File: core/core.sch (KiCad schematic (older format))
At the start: 9 parts, among them U1 BNO055

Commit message: Updated core with IMU and altimiter as specified on pinout
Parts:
- added C15, C16: 100nF, symbol Device:C
- added NT1: Net-Tie_2, symbol Device:Net-Tie_2
- added R6, R7: 4.7k, symbol Device:R
- added U3: BMP388, calstar:BMP388, symbol calstar:BMP388
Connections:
- net labels added: +3.3V, CSB, INT_ALT, INT_IMU
- net labels removed: INT, VDD, VDDIO
- wire segments 51 -> 89
- no-connect marks 52 -> 47
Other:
- moved on the sheet: C3, R2

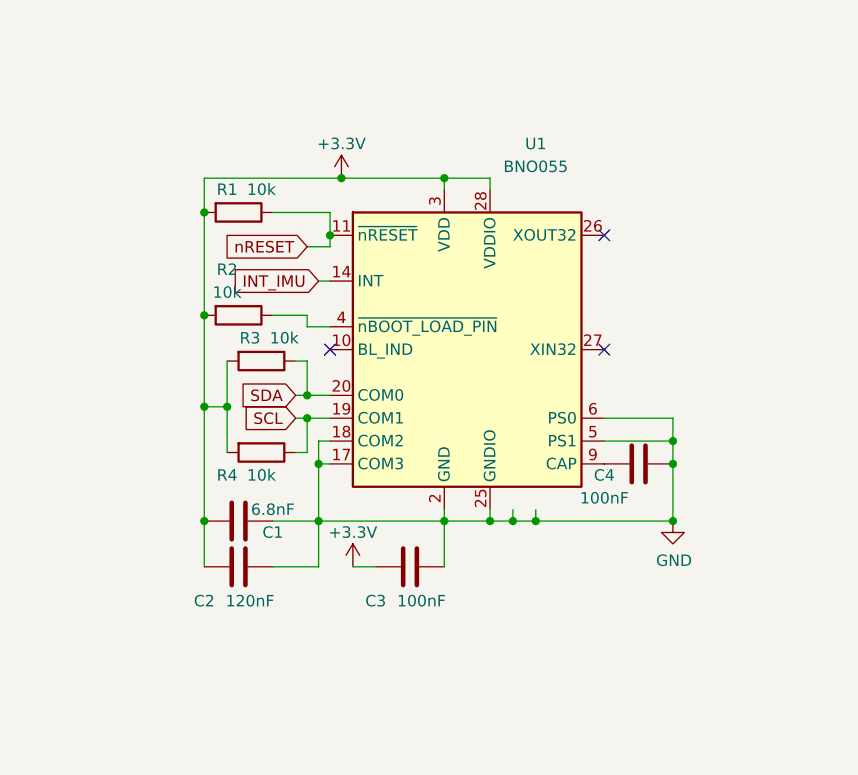
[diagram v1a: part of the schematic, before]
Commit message: Updated core with IMU hierarchical block
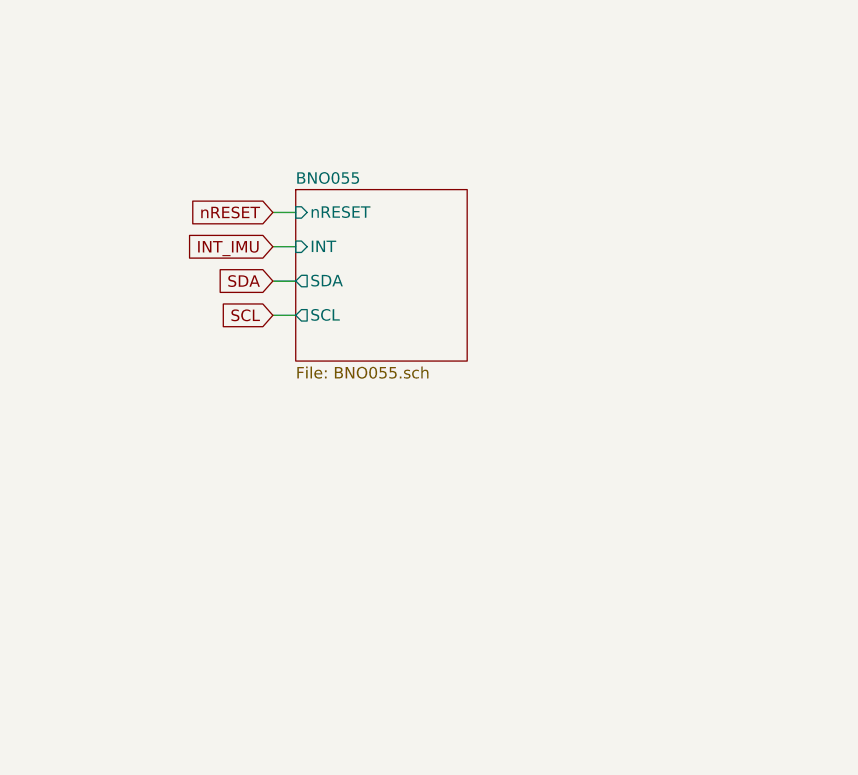
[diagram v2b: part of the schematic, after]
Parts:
- removed C1: 6.8nF, Capacitor_SMD:C_0603_1608Metric, symbol Device:C
- removed C2: 120nF, Capacitor_SMD:C_0603_1608Metric, symbol Device:C
- removed C3, C4: 100nF, Capacitor_SMD:C_0603_1608Metric, symbol Device:C
- removed R1, R2, R3, R4: 10k, Resistor_SMD:R_0603_1608Metric, symbol Device:R
- removed U1: BNO055, Package_LGA:LGA-28_5.2x3.8mm_P0.5mm, symbol Sensor_Motion:BNO055
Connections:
- wire segments 89 -> 41
- no-connect marks 47 -> 44

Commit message: Updated core with altimeter hierarchical block
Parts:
- removed C15, C16: 100nF, symbol Device:C
- removed NT1: Net-Tie_2, symbol Device:Net-Tie_2
- removed R6, R7: 4.7k, symbol Device:R
- removed U3: BMP388, calstar:BMP388, symbol calstar:BMP388
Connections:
- net labels removed: +3.3V, GND
- wire segments 41 -> 14
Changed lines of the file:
@@
 $Descr A4 11693 8268
 encoding utf-8
-Sheet 1 3
+Sheet 1 4
 Title ""
 Date ""
@@
 NoConn ~ 7500 4900
 NoConn ~ 7500 5050
-$Comp
-L calstar:BMP388 U3
-U 1 1 5E642E69
-P 3000 5750
-F 0 "U3" H 3000 6225 50  0000 C CNN
-F 1 "BMP388" H 3000 6134 50  0000 C CNN
-F 2 "calstar:BMP388" H 3000 6300 50  0001 C CNN
-F 3 "" H 3000 6150 50  0001 C CNN
-	1    3000 5750
-	1    0    0    -1
-$EndComp
-$Comp
-L Device:Net-Tie_2 NT1
-U 1 1 5E6430B0
-P 3450 5700
-F 0 "NT1" H 3600 5850 50  0000 C CNN
-F 1 "Net-Tie_2" H 3550 5750 50  0000 C CNN
-F 2 "" H 3450 5700 50  0001 C CNN
-F 3 "~" H 3450 5700 50  0001 C CNN
-	1    3450 5700
-	1    0    0    -1
-$EndComp
-$Comp
-L Device:R R6
-U 1 1 5E64313E
-P 3400 6100
-F 0 "R6" H 3470 6146 50  0000 L CNN
-F 1 "4.7k" H 3470 6055 50  0000 L CNN
-F 2 "" V 3330 6100 50  0001 C CNN
-F 3 "~" H 3400 6100 50  0001 C CNN
-	1    3400 6100
-	1    0    0    -1
-$EndComp
-$Comp
-L power:GND #PWR0114
-U 1 1 5E6431CF
-P 3550 5700
-F 0 "#PWR0114" H 3550 5450 50  0001 C CNN
-F 1 "GND" H 3400 5650 50  0000 C CNN
-F 2 "" H 3550 5700 50  0001 C CNN
-F 3 "" H 3550 5700 50  0001 C CNN
-	1    3550 5700
-	1    0    0    -1
-$EndComp
-Wire Wire Line
-	3350 5800 3450 5800
-Wire Wire Line
-	3450 5800 3450 5850
-Wire Wire Line
-	3800 5850 3800 5800
-Wire Wire Line
-	3450 5850 3800 5850
-$Comp
-L Device:R R7
-U 1 1 5E644FB0
-P 3800 5650
-F 0 "R7" H 3870 5696 50  0000 L CNN
-F 1 "4.7k" H 3870 5605 50  0000 L CNN
-F 2 "" V 3730 5650 50  0001 C CNN
-F 3 "~" H 3800 5650 50  0001 C CNN
-	1    3800 5650
-	1    0    0    -1
-$EndComp
-Wire Wire Line
-	3350 5900 3400 5900
-Wire Wire Line
-	3400 5900 3400 5950
-Text GLabel 3500 5450 2    50   Output ~ 0
+Text GLabel 2900 5400 0    50   Input ~ 0
 CSB
-Wire Wire Line
-	3450 5600 3450 5450
-Wire Wire Line
-	3450 5450 3500 5450
-Text GLabel 3500 5200 2    50   Input ~ 0
+Text GLabel 2900 5250 0    50   Input ~ 0
 INT_ALT
-Wire Wire Line
-	3500 5200 3400 5200
-Wire Wire Line
-	3400 5500 3350 5500
-Text GLabel 3850 5850 2    50   Input ~ 0
+Text GLabel 2900 5550 0    50   Input ~ 0
 SDA
-Wire Wire Line
-	3850 5850 3800 5850
-Connection ~ 3800 5850
-Text GLabel 3550 5950 2    50   Input ~ 0
+Text GLabel 3700 5550 2    50   Input ~ 0
 SCL
-Wire Wire Line
-	3550 5950 3400 5950
-Connection ~ 3400 5950
-Wire Wire Line
-	3800 5500 3800 5450
-$Comp
-L Device:C C16
-U 1 1 5E66780A
-P 2400 5550
-F 0 "C16" H 2650 5500 50  0000 R CNN
-F 1 "100nF" H 2650 5650 50  0000 R CNN
-F 2 "" H 2438 5400 50  0001 C CNN
-F 3 "~" H 2400 5550 50  0001 C CNN
-	1    2400 5550
-	-1   0    0    1
-$EndComp
-Wire Wire Line
-	2650 5600 2550 5600
-Wire Wire Line
-	2550 5600 2550 5500
-Wire Wire Line
-	2400 5700 2450 5700
-$Comp
-L power:GND #PWR0117
-U 1 1 5E66C6EE
-P 2450 5700
-F 0 "#PWR0117" H 2450 5450 50  0001 C CNN
-F 1 "GND" H 2300 5650 50  0000 C CNN
-F 2 "" H 2450 5700 50  0001 C CNN
-F 3 "" H 2450 5700 50  0001 C CNN
-	1    2450 5700
-	1    0    0    -1
-$EndComp
-Connection ~ 2450 5700
-Wire Wire Line
-	2450 5700 2650 5700
-Wire Wire Line
-	2650 5800 2550 5800
-Wire Wire Line
-	2550 5800 2550 5900
-Wire Wire Line
-	2550 5900 2650 5900
-Wire Wire Line
-	2550 5900 2250 5900
-Connection ~ 2550 5900
-$Comp
-L power:GND #PWR0118
-U 1 1 5E6708C1
-P 2250 5900
-F 0 "#PWR0118" H 2250 5650 50  0001 C CNN
-F 1 "GND" H 2250 5750 50  0000 C CNN
-F 2 "" H 2250 5900 50  0001 C CNN
-F 3 "" H 2250 5900 50  0001 C CNN
-	1    2250 5900
-	1    0    0    -1
-$EndComp
-Connection ~ 2250 5900
-Wire Wire Line
-	2250 5900 2000 5900
-$Comp
-L power:+3.3V #PWR0119
-U 1 1 5E67091E
-P 2000 5400
-F 0 "#PWR0119" H 2000 5250 50  0001 C CNN
-F 1 "+3.3V" H 2000 5550 50  0000 C CNN
-F 2 "" H 2000 5400 50  0001 C CNN
-F 3 "" H 2000 5400 50  0001 C CNN
-	1    2000 5400
-	1    0    0    -1
-$EndComp
-$Comp
-L Device:C C15
-U 1 1 5E670962
-P 2000 5650
-F 0 "C15" H 2200 5550 50  0000 R CNN
-F 1 "100nF" H 2250 5750 50  0000 R CNN
-F 2 "" H 2038 5500 50  0001 C CNN
-F 3 "~" H 2000 5650 50  0001 C CNN
-	1    2000 5650
-	-1   0    0    1
-$EndComp
-Wire Wire Line
-	2000 5900 2000 5800
-Wire Wire Line
-	3450 5600 3350 5600
 Text GLabel 8550 4600 2    50   Input ~ 0
 SDA
 Wire Wire Line
 	8550 4600 8400 4600
-$Comp
-L power:+3.3V #PWR0120
-U 1 1 5E67FDC2
-P 3800 5450
-F 0 "#PWR0120" H 3800 5300 50  0001 C CNN
-F 1 "+3.3V" H 3800 5600 50  0000 C CNN
-F 2 "" H 3800 5450 50  0001 C CNN
-F 3 "" H 3800 5450 50  0001 C CNN
-	1    3800 5450
-	1    0    0    -1
-$EndComp
-$Comp
-L power:+3.3V #PWR0121
-U 1 1 5E67FDEB
-P 3200 6250
-F 0 "#PWR0121" H 3200 6100 50  0001 C CNN
-F 1 "+3.3V" H 3200 6400 50  0000 C CNN
-F 2 "" H 3200 6250 50  0001 C CNN
-F 3 "" H 3200 6250 50  0001 C CNN
-	1    3200 6250
-	1    0    0    -1
-$EndComp
-Wire Wire Line
-	3400 6250 3200 6250
-Wire Wire Line
-	3400 5200 3400 5500
 Text GLabel 8550 3850 2    50   Input ~ 0
 INT_ALT
 Wire Wire Line
 	8550 3850 8400 3850
-Wire Wire Line
-	2550 5500 2650 5500
-Connection ~ 2550 5500
-Wire Wire Line
-	2550 5500 2550 5400
-Wire Wire Line
-	2400 5400 2550 5400
-Wire Wire Line
-	2400 5400 2000 5400
-Connection ~ 2400 5400
-Wire Wire Line
-	2000 5400 2000 5500
-Connection ~ 2000 5400
 $Sheet
 S 7500 1500 900  4100
@@
 Wire Wire Line
 	2900 2700 3000 2700
+$Sheet
+S 3100 5150 500  500
+U 5E6CF5BB
+F0 "BMP388_I2C" 50
+F1 "BMP388_I2C.sch" 50
+F2 "INT" I L 3100 5250 50
+F3 "CSB" I L 3100 5400 50
+F4 "SDA" O L 3100 5550 50
+F5 "SCL" O R 3600 5550 50
+$EndSheet
+Wire Wire Line
+	3100 5250 2900 5250
+Wire Wire Line
+	2900 5400 3100 5400
+Wire Wire Line
+	3100 5550 2900 5550
+Wire Wire Line
+	3700 5550 3600 5550
 $EndSCHEMATC

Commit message: added connector to core and determined pinout
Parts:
- added J?: FTMH-120-03-F-DV-P, symbol star-common-lib:FTMH-120-03-F-DV-P
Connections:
- net labels added: GND, I2C_SCL, I2C_SDA, IO_38, IO_39, SPI_MISO, SPI_MOSI, SPI_SCK, SPI_nSS1, SPI_nSS10, SPI_nSS11, SPI_nSS12, SPI_nSS13, SPI_nSS14, SPI_nSS15, SPI_nSS16, SPI_nSS2, SPI_nSS3, SPI_nSS4, SPI_nSS5, SPI_nSS6, SPI_nSS7, SPI_nSS8, SPI_nSS9, V1.2, V3.3, V5, V7.4
- net labels removed: SCL, SDA
- wire segments 14 -> 18
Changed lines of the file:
@@
 EESchema Schematic File Version 4
-LIBS:core-cache
-EELAYER 26 0
+EELAYER 30 0
 EELAYER END
 $Descr A4 11693 8268
@@
 Comment4 ""
 $EndDescr
-Text GLabel 2900 2700 0    50   Input ~ 0
-SCL
-Text GLabel 2900 2550 0    50   Input ~ 0
-SDA
-Text GLabel 2900 2400 0    50   Input ~ 0
-INT_IMU
-Text GLabel 2900 2250 0    50   Input ~ 0
-nRESET
-Text GLabel 8550 4000 2    50   Input ~ 0
-CSB
-Text GLabel 7350 3400 0    50   Input ~ 0
-SCL
 Wire Wire Line
 	7350 3400 7500 3400
@@
 NoConn ~ 7500 4900
 NoConn ~ 7500 5050
-Text GLabel 2900 5400 0    50   Input ~ 0
-CSB
-Text GLabel 2900 5250 0    50   Input ~ 0
-INT_ALT
-Text GLabel 2900 5550 0    50   Input ~ 0
-SDA
-Text GLabel 3700 5550 2    50   Input ~ 0
-SCL
-Text GLabel 8550 4600 2    50   Input ~ 0
-SDA
 Wire Wire Line
 	8550 4600 8400 4600
-Text GLabel 8550 3850 2    50   Input ~ 0
-INT_ALT
 Wire Wire Line
 	8550 3850 8400 3850
@@
 F52 "PH1" I L 7500 5050 50
 $EndSheet
-Text GLabel 8550 3250 2    50   Input ~ 0
-nRESET
-Text GLabel 8550 3400 2    50   Input ~ 0
-INT_IMU
 Wire Wire Line
 	8550 3250 8400 3250
@@
 Wire Wire Line
 	3700 5550 3600 5550
+$Comp
+L star-common-lib:FTMH-120-03-F-DV-P J?
+U 1 1 5E646F14
+P 5400 2850
+F 0 "J?" H 5450 3967 50  0000 C CNN
+F 1 "FTMH-120-03-F-DV-P" H 5450 3876 50  0000 C CNN
+F 2 "" H 5400 2850 50  0001 C CNN
+F 3 "~" H 5400 2850 50  0001 C CNN
+	1    5400 2850
+	1    0    0    -1
+$EndComp
+Text Label 7350 3400 2    50   ~ 0
+I2C_SCL
+Text Label 2900 2250 2    50   ~ 0
+nRESET
+Text Label 2900 2400 2    50   ~ 0
+INT_IMU
+Text Label 2900 2550 2    50   ~ 0
+I2C_SDA
+Text Label 2900 2700 2    50   ~ 0
+I2C_SCL
+Text Label 2900 5250 2    50   ~ 0
+INT_ALT
+Text Label 2900 5400 2    50   ~ 0
+CSB
+Text Label 2900 5550 2    50   ~ 0
+I2C_SDA
+Text Label 3700 5550 0    50   ~ 0
+I2C_SCL
+Text Label 8550 3250 0    50   ~ 0
+nRESET
+Text Label 8550 3400 0    50   ~ 0
+INT_IMU
+Text Label 8550 3850 0    50   ~ 0
+INT_ALT
+Text Label 8550 4000 0    50   ~ 0
+CSB
+Text Label 8550 4600 0    50   ~ 0
+I2C_SDA
+Text Label 5700 3750 0    50   ~ 0
+IO_38
+Text Label 5200 2050 2    50   ~ 0
+SPI_MISO
+Text Label 5200 2150 2    50   ~ 0
+SPI_nSS1
+Text Label 5200 2250 2    50   ~ 0
+SPI_nSS3
+Text Label 5200 2350 2    50   ~ 0
+SPI_nSS5
+Text Label 5200 2450 2    50   ~ 0
+SPI_nSS7
+Text Label 5200 2550 2    50   ~ 0
+SPI_nSS9
+Text Label 5200 2650 2    50   ~ 0
+SPI_nSS11
+Text Label 5200 2750 2    50   ~ 0
+SPI_nSS13
+Text Label 5200 2850 2    50   ~ 0
+SPI_nSS15
+Text Label 5700 1950 0    50   ~ 0
+SPI_SCK
+Text Label 5700 2050 0    50   ~ 0
+SPI_MOSI
+Text Label 5700 2150 0    50   ~ 0
+SPI_nSS2
+Text Label 5700 2250 0    50   ~ 0
+SPI_nSS4
+Text Label 5700 2350 0    50   ~ 0
+SPI_nSS6
+Text Label 5700 2450 0    50   ~ 0
+SPI_nSS8
+Text Label 5700 2550 0    50   ~ 0
+SPI_nSS10
+Text Label 5700 2650 0    50   ~ 0
+SPI_nSS12
+Text Label 5700 2750 0    50   ~ 0
+SPI_nSS14
+Text Label 5200 2950 2    50   ~ 0
+V3.3
+Text Label 5200 3050 2    50   ~ 0
+V5
+Text Label 5700 2850 0    50   ~ 0
+SPI_nSS16
+Text Label 5700 3050 0    50   ~ 0
+V7.4
+$Comp
+L power:GND #PWR?
+U 1 1 5E652AC2
+P 6250 2950
+F 0 "#PWR?" H 6250 2700 50  0001 C CNN
+F 1 "GND" H 6255 2777 50  0000 C CNN
+F 2 "" H 6250 2950 50  0001 C CNN
+F 3 "" H 6250 2950 50  0001 C CNN
+	1    6250 2950
+	1    0    0    -1
+$EndComp
+Wire Wire Line
+	5700 2950 6250 2950
+Text Label 5200 3850 2    50   ~ 0
+IO_39
+Text Label 5200 3250 2    50   ~ 0
+I2C_SCL
+Text Label 5700 3250 0    50   ~ 0
+I2C_SDA
+$Comp
+L power:GND #PWR?
+U 1 1 5E65479A
+P 4700 1950
+F 0 "#PWR?" H 4700 1700 50  0001 C CNN
+F 1 "GND" H 4705 1777 50  0000 C CNN
+F 2 "" H 4700 1950 50  0001 C CNN
+F 3 "" H 4700 1950 50  0001 C CNN
+	1    4700 1950
+	1    0    0    -1
+$EndComp
+Wire Wire Line
+	4700 1950 5200 1950
+Text Label 5200 3150 2    50   ~ 0
+V1.2
+$Comp
+L power:GND #PWR?
+U 1 1 5E656A75
+P 6250 3850
+F 0 "#PWR?" H 6250 3600 50  0001 C CNN
+F 1 "GND" H 6255 3677 50  0000 C CNN
+F 2 "" H 6250 3850 50  0001 C CNN
+F 3 "" H 6250 3850 50  0001 C CNN
+	1    6250 3850
+	1    0    0    -1
+$EndComp
+Wire Wire Line
+	6250 3850 5700 3850
+Wire Wire Line
+	4700 3350 5200 3350
+$Comp
+L power:GND #PWR?
+U 1 1 5E657C0D
+P 4700 3350
+F 0 "#PWR?" H 4700 3100 50  0001 C CNN
+F 1 "GND" H 4705 3177 50  0000 C CNN
+F 2 "" H 4700 3350 50  0001 C CNN
+F 3 "" H 4700 3350 50  0001 C CNN
+	1    4700 3350
+	1    0    0    -1
+$EndComp
+Text Label 5700 3350 0    50   ~ 0
+V3.3
+Text Label 5700 3150 0    50   ~ 0
+V5
 $EndSCHEMATC

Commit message: bump hardware-sch-blocks pre-PR
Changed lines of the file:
@@
 Wire Wire Line
 	8550 3850 8400 3850
+Wire Wire Line
+	8550 3250 8400 3250
+Wire Wire Line
+	8400 3400 8550 3400
+Wire Wire Line
+	3000 2250 2900 2250
+Wire Wire Line
+	2900 2400 3000 2400
+Wire Wire Line
+	3000 2550 2900 2550
+Wire Wire Line
+	2900 2700 3000 2700
+Wire Wire Line
+	3100 5250 2900 5250
+Wire Wire Line
+	2900 5400 3100 5400
+Wire Wire Line
+	3100 5550 2900 5550
+Wire Wire Line
+	3700 5550 3600 5550
+$Comp
+L star-common-lib:FTMH-120-03-F-DV-P J?
+U 1 1 5E646F14
+P 5400 2850
+F 0 "J?" H 5450 3967 50  0000 C CNN
+F 1 "FTMH-120-03-F-DV-P" H 5450 3876 50  0000 C CNN
+F 2 "" H 5400 2850 50  0001 C CNN
+F 3 "~" H 5400 2850 50  0001 C CNN
+	1    5400 2850
+	1    0    0    -1
+$EndComp
+Text Label 7350 3400 2    50   ~ 0
+I2C_SCL
+Text Label 2900 2250 2    50   ~ 0
+nRESET
+Text Label 2900 2400 2    50   ~ 0
+INT_IMU
+Text Label 2900 2550 2    50   ~ 0
+I2C_SDA
+Text Label 2900 2700 2    50   ~ 0
+I2C_SCL
+Text Label 2900 5250 2    50   ~ 0
+INT_ALT
+Text Label 2900 5400 2    50   ~ 0
+CSB
+Text Label 2900 5550 2    50   ~ 0
+I2C_SDA
+Text Label 3700 5550 0    50   ~ 0
+I2C_SCL
+Text Label 8550 3250 0    50   ~ 0
+nRESET
+Text Label 8550 3400 0    50   ~ 0
+INT_IMU
+Text Label 8550 3850 0    50   ~ 0
+INT_ALT
+Text Label 8550 4000 0    50   ~ 0
+CSB
+Text Label 8550 4600 0    50   ~ 0
+I2C_SDA
+Text Label 5700 3750 0    50   ~ 0
+IO_38
+Text Label 5200 2050 2    50   ~ 0
+SPI_MISO
+Text Label 5200 2150 2    50   ~ 0
+SPI_nSS1
+Text Label 5200 2250 2    50   ~ 0
+SPI_nSS3
+Text Label 5200 2350 2    50   ~ 0
+SPI_nSS5
+Text Label 5200 2450 2    50   ~ 0
+SPI_nSS7
+Text Label 5200 2550 2    50   ~ 0
+SPI_nSS9
+Text Label 5200 2650 2    50   ~ 0
+SPI_nSS11
+Text Label 5200 2750 2    50   ~ 0
+SPI_nSS13
+Text Label 5200 2850 2    50   ~ 0
+SPI_nSS15
+Text Label 5700 1950 0    50   ~ 0
+SPI_SCK
+Text Label 5700 2050 0    50   ~ 0
+SPI_MOSI
+Text Label 5700 2150 0    50   ~ 0
+SPI_nSS2
+Text Label 5700 2250 0    50   ~ 0
+SPI_nSS4
+Text Label 5700 2350 0    50   ~ 0
+SPI_nSS6
+Text Label 5700 2450 0    50   ~ 0
+SPI_nSS8
+Text Label 5700 2550 0    50   ~ 0
+SPI_nSS10
+Text Label 5700 2650 0    50   ~ 0
+SPI_nSS12
+Text Label 5700 2750 0    50   ~ 0
+SPI_nSS14
+Text Label 5200 2950 2    50   ~ 0
+V3.3
+Text Label 5200 3050 2    50   ~ 0
+V5
+Text Label 5700 2850 0    50   ~ 0
+SPI_nSS16
+Text Label 5700 3050 0    50   ~ 0
+V7.4
+$Comp
+L power:GND #PWR?
+U 1 1 5E652AC2
+P 6250 2950
+F 0 "#PWR?" H 6250 2700 50  0001 C CNN
+F 1 "GND" H 6255 2777 50  0000 C CNN
+F 2 "" H 6250 2950 50  0001 C CNN
+F 3 "" H 6250 2950 50  0001 C CNN
+	1    6250 2950
+	1    0    0    -1
+$EndComp
+Wire Wire Line
+	5700 2950 6250 2950
+Text Label 5200 3850 2    50   ~ 0
+IO_39
+Text Label 5200 3250 2    50   ~ 0
+I2C_SCL
+Text Label 5700 3250 0    50   ~ 0
+I2C_SDA
+$Comp
+L power:GND #PWR?
+U 1 1 5E65479A
+P 4700 1950
+F 0 "#PWR?" H 4700 1700 50  0001 C CNN
+F 1 "GND" H 4705 1777 50  0000 C CNN
+F 2 "" H 4700 1950 50  0001 C CNN
+F 3 "" H 4700 1950 50  0001 C CNN
+	1    4700 1950
+	1    0    0    -1
+$EndComp
+Wire Wire Line
+	4700 1950 5200 1950
+Text Label 5200 3150 2    50   ~ 0
+V1.2
+$Comp
+L power:GND #PWR?
+U 1 1 5E656A75
+P 6250 3850
+F 0 "#PWR?" H 6250 3600 50  0001 C CNN
+F 1 "GND" H 6255 3677 50  0000 C CNN
+F 2 "" H 6250 3850 50  0001 C CNN
+F 3 "" H 6250 3850 50  0001 C CNN
+	1    6250 3850
+	1    0    0    -1
+$EndComp
+Wire Wire Line
+	6250 3850 5700 3850
+Wire Wire Line
+	4700 3350 5200 3350
+$Comp
+L power:GND #PWR?
+U 1 1 5E657C0D
+P 4700 3350
+F 0 "#PWR?" H 4700 3100 50  0001 C CNN
+F 1 "GND" H 4705 3177 50  0000 C CNN
+F 2 "" H 4700 3350 50  0001 C CNN
+F 3 "" H 4700 3350 50  0001 C CNN
+	1    4700 3350
+	1    0    0    -1
+$EndComp
+Text Label 5700 3350 0    50   ~ 0
+V3.3
+Text Label 5700 3150 0    50   ~ 0
+V5
 $Sheet
 S 7500 1500 900  4100
 U 5E52591C
 F0 "STM32F401RET6" 50
-F1 "STM32F401RET6.sch" 50
+F1 "hardware-sch-blocks/STM32F401RET6/STM32F401RET6.sch" 50
 F2 "nRST" I L 7500 1600 50
 F3 "SWDIO" I L 7500 1750 50
@@
 F52 "PH1" I L 7500 5050 50
 $EndSheet
-Wire Wire Line
-	8550 3250 8400 3250
-Wire Wire Line
-	8400 3400 8550 3400
 $Sheet
 S 3000 2150 750  750
 U 5E6B2FC0
 F0 "BNO055" 50
-F1 "BNO055.sch" 50
+F1 "hardware-sch-blocks/BNO055/BNO055.sch" 50
 F2 "nRESET" I L 3000 2250 50
 F3 "INT" I L 3000 2400 50
@@
 F5 "SCL" O L 3000 2700 50
 $EndSheet
-Wire Wire Line
-	3000 2250 2900 2250
-Wire Wire Line
-	2900 2400 3000 2400
-Wire Wire Line
-	3000 2550 2900 2550
-Wire Wire Line
-	2900 2700 3000 2700
 $Sheet
 S 3100 5150 500  500
 U 5E6CF5BB
 F0 "BMP388_I2C" 50
-F1 "BMP388_I2C.sch" 50
+F1 "hardware-sch-blocks/BMP388_I2C/BMP388_I2C.sch" 50
 F2 "INT" I L 3100 5250 50
 F3 "CSB" I L 3100 5400 50
@@
 F5 "SCL" O R 3600 5550 50
 $EndSheet
-Wire Wire Line
-	3100 5250 2900 5250
-Wire Wire Line
-	2900 5400 3100 5400
-Wire Wire Line
-	3100 5550 2900 5550
-Wire Wire Line
-	3700 5550 3600 5550
-$Comp
-L star-common-lib:FTMH-120-03-F-DV-P J?
-U 1 1 5E646F14
-P 5400 2850
-F 0 "J?" H 5450 3967 50  0000 C CNN
-F 1 "FTMH-120-03-F-DV-P" H 5450 3876 50  0000 C CNN
-F 2 "" H 5400 2850 50  0001 C CNN
-F 3 "~" H 5400 2850 50  0001 C CNN
-	1    5400 2850
-	1    0    0    -1
-$EndComp
-Text Label 7350 3400 2    50   ~ 0
-I2C_SCL
-Text Label 2900 2250 2    50   ~ 0
-nRESET
-Text Label 2900 2400 2    50   ~ 0
-INT_IMU
-Text Label 2900 2550 2    50   ~ 0
-I2C_SDA
-Text Label 2900 2700 2    50   ~ 0
-I2C_SCL
-Text Label 2900 5250 2    50   ~ 0
-INT_ALT
-Text Label 2900 5400 2    50   ~ 0
-CSB
-Text Label 2900 5550 2    50   ~ 0
-I2C_SDA
-Text Label 3700 5550 0    50   ~ 0
-I2C_SCL
-Text Label 8550 3250 0    50   ~ 0
-nRESET
-Text Label 8550 3400 0    50   ~ 0
-INT_IMU
-Text Label 8550 3850 0    50   ~ 0
-INT_ALT
-Text Label 8550 4000 0    50   ~ 0
-CSB
-Text Label 8550 4600 0    50   ~ 0
-I2C_SDA
-Text Label 5700 3750 0    50   ~ 0
-IO_38
-Text Label 5200 2050 2    50   ~ 0
-SPI_MISO
-Text Label 5200 2150 2    50   ~ 0
-SPI_nSS1
-Text Label 5200 2250 2    50   ~ 0
-SPI_nSS3
-Text Label 5200 2350 2    50   ~ 0
-SPI_nSS5
-Text Label 5200 2450 2    50   ~ 0
-SPI_nSS7
-Text Label 5200 2550 2    50   ~ 0
-SPI_nSS9
-Text Label 5200 2650 2    50   ~ 0
-SPI_nSS11
-Text Label 5200 2750 2    50   ~ 0
-SPI_nSS13
-Text Label 5200 2850 2    50   ~ 0
-SPI_nSS15
-Text Label 5700 1950 0    50   ~ 0
-SPI_SCK
-Text Label 5700 2050 0    50   ~ 0
-SPI_MOSI
-Text Label 5700 2150 0    50   ~ 0
-SPI_nSS2
-Text Label 5700 2250 0    50   ~ 0
-SPI_nSS4
-Text Label 5700 2350 0    50   ~ 0
-SPI_nSS6
-Text Label 5700 2450 0    50   ~ 0
-SPI_nSS8
-Text Label 5700 2550 0    50   ~ 0
-SPI_nSS10
-Text Label 5700 2650 0    50   ~ 0
-SPI_nSS12
-Text Label 5700 2750 0    50   ~ 0
-SPI_nSS14
-Text Label 5200 2950 2    50   ~ 0
-V3.3
-Text Label 5200 3050 2    50   ~ 0
-V5
-Text Label 5700 2850 0    50   ~ 0
-SPI_nSS16
-Text Label 5700 3050 0    50   ~ 0
-V7.4
-$Comp
-L power:GND #PWR?
-U 1 1 5E652AC2
-P 6250 2950
-F 0 "#PWR?" H 6250 2700 50  0001 C CNN
-F 1 "GND" H 6255 2777 50  0000 C CNN
-F 2 "" H 6250 2950 50  0001 C CNN
-F 3 "" H 6250 2950 50  0001 C CNN
-	1    6250 2950
-	1    0    0    -1
-$EndComp
-Wire Wire Line
-	5700 2950 6250 2950
-Text Label 5200 3850 2    50   ~ 0
-IO_39
-Text Label 5200 3250 2    50   ~ 0
-I2C_SCL
-Text Label 5700 3250 0    50   ~ 0
-I2C_SDA
-$Comp
-L power:GND #PWR?
-U 1 1 5E65479A
-P 4700 1950
-F 0 "#PWR?" H 4700 1700 50  0001 C CNN
-F 1 "GND" H 4705 1777 50  0000 C CNN
-F 2 "" H 4700 1950 50  0001 C CNN
-F 3 "" H 4700 1950 50  0001 C CNN
-	1    4700 1950
-	1    0    0    -1
-$EndComp
-Wire Wire Line
-	4700 1950 5200 1950
-Text Label 5200 3150 2    50   ~ 0
-V1.2
-$Comp
-L power:GND #PWR?
-U 1 1 5E656A75
-P 6250 3850
-F 0 "#PWR?" H 6250 3600 50  0001 C CNN
-F 1 "GND" H 6255 3677 50  0000 C CNN
-F 2 "" H 6250 3850 50  0001 C CNN
-F 3 "" H 6250 3850 50  0001 C CNN
-	1    6250 3850
-	1    0    0    -1
-$EndComp
-Wire Wire Line
-	6250 3850 5700 3850
-Wire Wire Line
-	4700 3350 5200 3350
-$Comp
-L power:GND #PWR?
-U 1 1 5E657C0D
-P 4700 3350
-F 0 "#PWR?" H 4700 3100 50  0001 C CNN
-F 1 "GND" H 4705 3177 50  0000 C CNN
-F 2 "" H 4700 3350 50  0001 C CNN
-F 3 "" H 4700 3350 50  0001 C CNN
-	1    4700 3350
-	1    0    0    -1
-$EndComp
-Text Label 5700 3350 0    50   ~ 0
-V3.3
-Text Label 5700 3150 0    50   ~ 0
-V5
 $EndSCHEMATC

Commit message: Fix Aled's comments on PR #1
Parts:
- J?: symbol star-common-lib:FTMH-120-03-F-DV-P -> core-rescue:FTMH-120-03-F-DV-P-star-common-lib
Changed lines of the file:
@@
 	3700 5550 3600 5550
 $Comp
-L star-common-lib:FTMH-120-03-F-DV-P J?
+L core-rescue:FTMH-120-03-F-DV-P-star-common-lib J?
 U 1 1 5E646F14
 P 5400 2850
